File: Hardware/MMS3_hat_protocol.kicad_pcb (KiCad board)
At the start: 2 copper layers, 100 x 50 mm, 117 parts, among them J1 Chainbus in, J10 Conn_01x02_Pin, J11 Conn_01x04_Pin, J14 Conn_01x03_Pin, J15 Conn_01x04_Pin, J2 Chainbus Out, J3 Conn_01x02_Pin, J4 Conn_01x04_Pin, J5 Conn_01x03_Pin, J6 Conn_01x04_Pin, J7 Conn_01x06_Pin, J8 Conn_01x03_Pin, J9 Conn_01x04_Pin, U1 SN74CB3Q3384APW, U10 TXU0104PWR, U11 TXU0104PWR, U12 TXU0104PWR, U13 TCA9535PWR_C130204, U15 MAX13487EESA, U2 M24C64, U3 AMS1117, U4 TXU0104PWR, U5 TXU0104PWR, U6 MAX13487EESA, U8 TXU0104PWR, U9 PCA9306DCUR

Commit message: V1.1, added photo
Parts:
- removed H7, H8, H9: ~, PCM_JLCPCB:Hole_Tooling_JLCPCB
- turned D15 to 180 degrees
- turned D16 to 180 degrees
- turned D17 to 180 degrees
- turned D18 to 180 degrees
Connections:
- D15 pad 1: +3V3 -> Net-(D15-Pad1)
- D15 pad 2: Net-(D15-Pad2) -> +3V3
- D16 pad 1: +3V3 -> Net-(D16-Pad1)
- D16 pad 2: Net-(D16-Pad2) -> +3V3
- D17 pad 1: +3V3 -> Net-(D17-Pad1)
- D17 pad 2: Net-(D17-Pad2) -> +3V3
- D18 pad 1: +3V3 -> Net-(D18-Pad1)
- D18 pad 2: Net-(D18-Pad2) -> +3V3
- R37 pad 2: Net-(D15-Pad2) -> Net-(D15-Pad1)
- R39 pad 2: Net-(D16-Pad2) -> Net-(D16-Pad1)
- R41 pad 2: Net-(D17-Pad2) -> Net-(D17-Pad1)
- R43 pad 2: Net-(D18-Pad2) -> Net-(D18-Pad1)
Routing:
- net Net-(D16-Pad2): track 1.34 -> 0.00 mm
- net Net-(D16-Pad1): track 0.00 -> 1.34 mm
- net Net-(D15-Pad2): track 1.34 -> 0.00 mm
- net Net-(D15-Pad1): track 0.00 -> 1.34 mm
- net Net-(D18-Pad2): track 1.34 -> 0.00 mm
- net Net-(D18-Pad1): track 0.00 -> 1.34 mm
- net Net-(D17-Pad2): track 1.33 -> 0.00 mm
- net Net-(D17-Pad1): track 0.00 -> 1.33 mm
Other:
- board text added: "Version 1.1 Made by Wojciech Szafrański"
- board text removed: "Version 1.0 Made by Wojciech Szafrański"

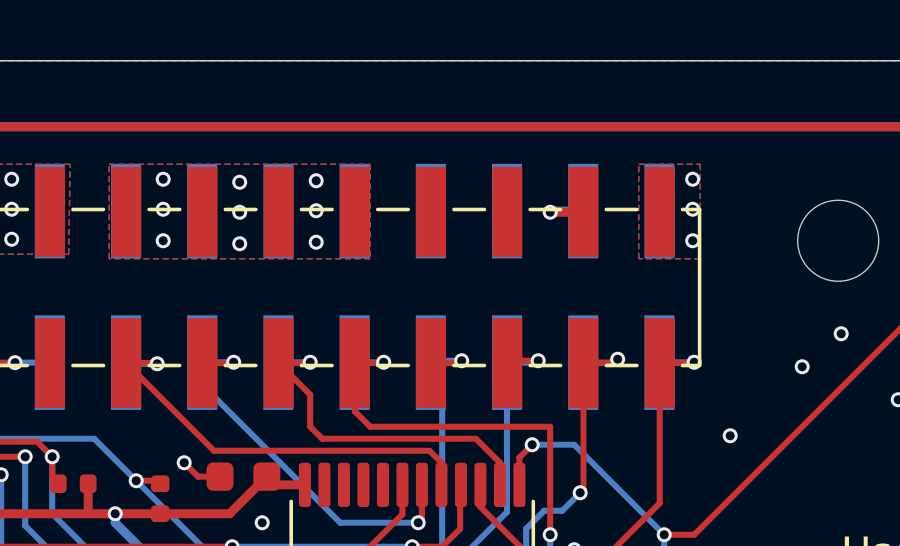
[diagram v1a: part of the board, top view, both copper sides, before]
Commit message: fixed reserved pins
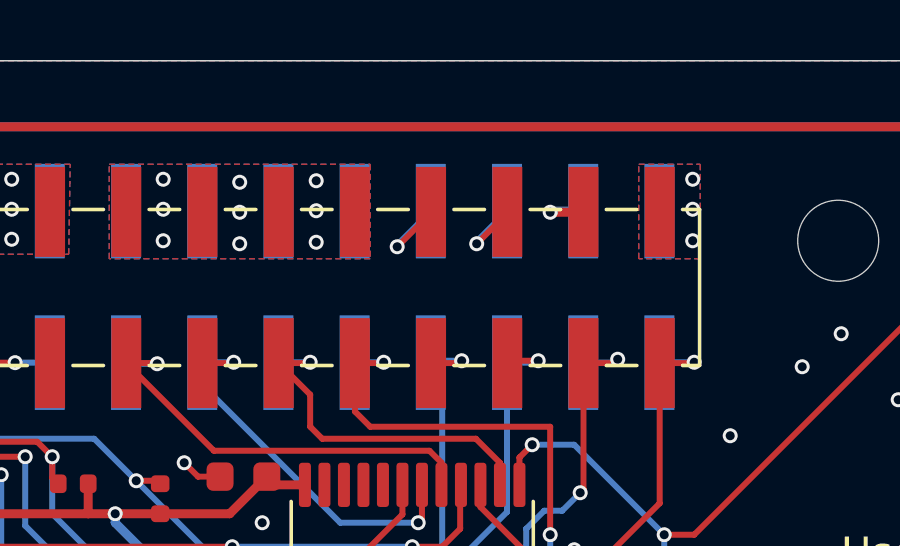
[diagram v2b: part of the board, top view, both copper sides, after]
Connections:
- J1 pad 25: unconnected-(J1-Pin_25-Pad25) -> /Interboard_connector/R1
- J1 pad 27: unconnected-(J1-Pin_27-Pad27) -> /Interboard_connector/R2
- J2 pad 25: unconnected-(J2-Pin_25-Pad25) -> /Interboard_connector/R1
- J2 pad 27: unconnected-(J2-Pin_27-Pad27) -> /Interboard_connector/R2
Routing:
- net /Interboard_connector/R1: track 0.00 -> 3.28 mm, vias 0 -> 1
- net /Interboard_connector/R2: track 0.00 -> 2.99 mm, vias 0 -> 1
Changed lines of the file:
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@@
 			(size 3 1)
 			(layers "F.Cu" "F.Mask" "F.Paste")
-			(net "unconnected-(J2-Pin_25-Pad25)")
+			(net "/Interboard_connector/R1")
 			(pinfunction "Pin_25_25")
-			(pintype "passive+no_connect")
+			(pintype "passive")
 		)
 		(pad "26" smd rect
@@
 			(size 3 1)
 			(layers "F.Cu" "F.Mask" "F.Paste")
-			(net "unconnected-(J2-Pin_27-Pad27)")
+			(net "/Interboard_connector/R2")
 			(pinfunction "Pin_27_27")
-			(pintype "passive+no_connect")
+			(pintype "passive")
 		)
 		(pad "28" smd rect
@@
 			(size 3.15 1)
 			(layers "B.Cu" "B.Mask" "B.Paste")
-			(net "unconnected-(J1-Pin_25-Pad25)")
+			(net "/Interboard_connector/R1")
 			(pinfunction "Pin_25_25")
-			(pintype "passive+no_connect")
+			(pintype "passive")
 		)
 		(pad "26" smd rect
@@
 			(size 3.15 1)
 			(layers "B.Cu" "B.Mask" "B.Paste")
-			(net "unconnected-(J1-Pin_27-Pad27)")
+			(net "/Interboard_connector/R2")
 			(pinfunction "Pin_27_27")
-			(pintype "passive+no_connect")
+			(pintype "passive")
 		)
 		(pad "28" smd rect
@@
 	)
 	(segment
+		(start 87.825 101.102)
+		(end 86.492 101.102)
+		(width 0.2)
+		(layer "F.Cu")
+		(net "Net-(D18-Pad1)")
+	)
+	(segment
+		(start 86.492 101.102)
+		(end 86.49 101.1)
+		(width 0.2)
+		(layer "F.Cu")
+		(net "Net-(D18-Pad1)")
+	)
+	(segment
 		(start 86.508 117.908)
 		(end 86.5 117.9)
@@
 	)
 	(segment
+		(start 86.483334 104.836667)
+		(end 86.48 104.833333)
+		(width 0.2)
+		(layer "F.Cu")
+		(net "Net-(D15-Pad1)")
+	)
+	(segment
+		(start 87.815 104.836667)
+		(end 86.483334 104.836667)
+		(width 0.2)
+		(layer "F.Cu")
+		(net "Net-(D15-Pad1)")
+	)
+	(segment
 		(start 158.1 130)
 		(end 159.1 131)
@@
 	)
 	(segment
+		(start 86.484 106.704)
+		(end 86.48 106.7)
+		(width 0.2)
+		(layer "F.Cu")
+		(net "Net-(D16-Pad1)")
+	)
+	(segment
+		(start 87.815 106.704)
+		(end 86.484 106.704)
+		(width 0.2)
+		(layer "F.Cu")
+		(net "Net-(D16-Pad1)")
+	)
+	(segment
 		(start 87.835 121.642667)
 		(end 86.509334 121.642667)
@@
 	)
 	(segment
+		(start 87.825 123.51)
+		(end 86.51 123.51)
+		(width 0.2)
+		(layer "F.Cu")
+		(net "Net-(D17-Pad1)")
+	)
+	(segment
+		(start 86.51 123.51)
+		(end 86.5 123.5)
+		(width 0.2)
+		(layer "F.Cu")
+		(net "Net-(D17-Pad1)")
+	)
+	(segment
 		(start 87.835 114.173333)
 		(end 86.506666 114.173333)
@@
 	)
 	(segment
-		(start 86.483334 104.836667)
-		(end 86.48 104.833333)
+		(start 139.43 93.038272)
+		(end 139.43 93.07)
 		(width 0.2)
 		(layer "F.Cu")
-		(net "Net-(D15-Pad1)")
+		(net "/Interboard_connector/R1")
 	)
 	(segment
-		(start 87.815 104.836667)
-		(end 86.483334 104.836667)
+		(start 139.43 93.07)
+		(end 138.3 94.2)
 		(width 0.2)
 		(layer "F.Cu")
-		(net "Net-(D15-Pad1)")
+		(net "/Interboard_connector/R1")
+	)
+	(via
+		(at 138.3 94.2)
+		(size 0.5)
+		(drill 0.3)
+		(layers "F.Cu" "B.Cu")
+		(net "/Interboard_connector/R1")
 	)
 	(segment
-		(start 86.484 106.704)
-		(end 86.48 106.7)
+		(start 138.3 94.133272)
+		(end 139.42 93.013272)
 		(width 0.2)
-		(layer "F.Cu")
-		(net "Net-(D16-Pad1)")
+		(layer "B.Cu")
+		(net "/Interboard_connector/R1")
 	)
 	(segment
-		(start 87.815 106.704)
-		(end 86.484 106.704)
+		(start 138.3 94.2)
+		(end 138.3 94.133272)
 		(width 0.2)
-		(layer "F.Cu")
-		(net "Net-(D16-Pad1)")
+		(layer "B.Cu")
+		(net "/Interboard_connector/R1")
 	)
 	(segment
-		(start 87.825 123.51)
-		(end 86.51 123.51)
+		(start 141.97 93.038272)
+		(end 141.97 93.08)
 		(width 0.2)
 		(layer "F.Cu")
-		(net "Net-(D17-Pad1)")
+		(net "/Interboard_connector/R2")
 	)
 	(segment
-		(start 86.51 123.51)
-		(end 86.5 123.5)
+		(start 141.97 93.08)
+		(end 140.95 94.1)
 		(width 0.2)
 		(layer "F.Cu")
-		(net "Net-(D17-Pad1)")
+		(net "/Interboard_connector/R2")
+	)
+	(via
+		(at 140.95 94.1)
+		(size 0.5)
+		(drill 0.3)
+		(layers "F.Cu" "B.Cu")
+		(net "/Interboard_connector/R2")
 	)
 	(segment
-		(start 87.825 101.102)
-		(end 86.492 101.102)
+		(start 140.95 94.023272)
+		(end 141.96 93.013272)
 		(width 0.2)
-		(layer "F.Cu")
-		(net "Net-(D18-Pad1)")
+		(layer "B.Cu")
+		(net "/Interboard_connector/R2")
 	)
 	(segment
-		(start 86.492 101.102)
-		(end 86.49 101.1)
+		(start 140.95 94.1)
+		(end 140.95 94.023272)
 		(width 0.2)
-		(layer "F.Cu")
-		(net "Net-(D18-Pad1)")
+		(layer "B.Cu")
+		(net "/Interboard_connector/R2")
 	)
 	(zone
